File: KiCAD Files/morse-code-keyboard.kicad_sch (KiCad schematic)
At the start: 10 parts, among them IC2 USBLC6-2SC6, J1 UJ32-C-H-G-H2-SMT-TR, SW1 SW_Push, SW2 SW_Push, SW3 SW_Push, SW4 SW_Push, SW8 SW_Push, SW9 SW_Push

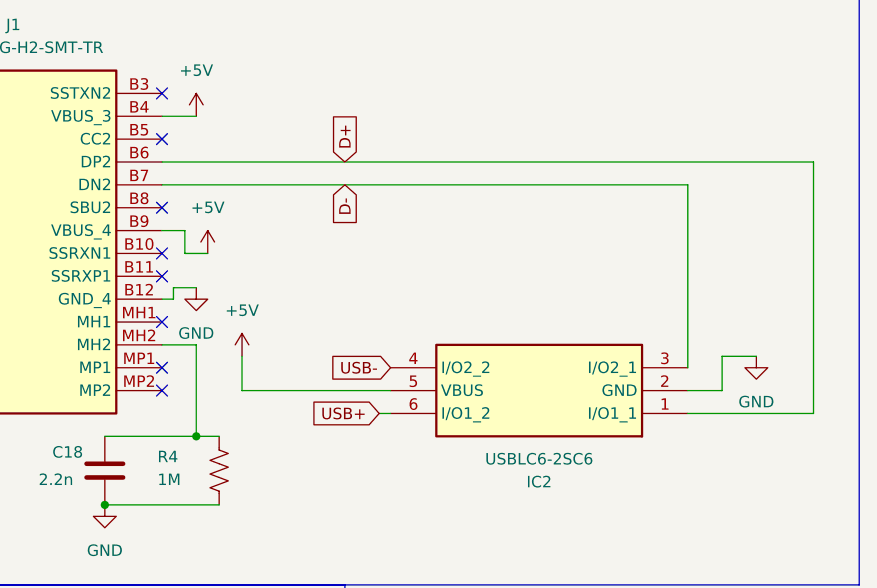
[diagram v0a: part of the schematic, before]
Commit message: changed out microcontroller
Might add in a bit of debug circuitry + button leds will see tmmrw
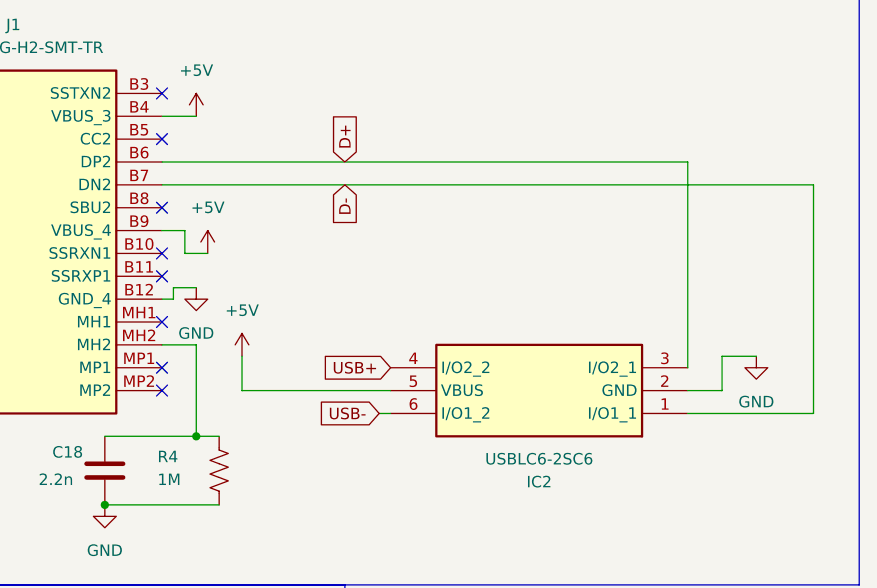
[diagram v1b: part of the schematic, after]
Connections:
- net D+: now also IC2.3 (I/O2_1); no longer IC2.1 (I/O1_1)
- net D-: now also IC2.1 (I/O1_1); no longer IC2.3 (I/O2_1)
- net USB+: now also IC2.4 (I/O2_2); no longer IC2.6 (I/O1_2)
- net USB-: now also IC2.6 (I/O1_2); no longer IC2.4 (I/O2_2)
